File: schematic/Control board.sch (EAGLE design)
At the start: 14 parts, among them IC2 ATTINY44A

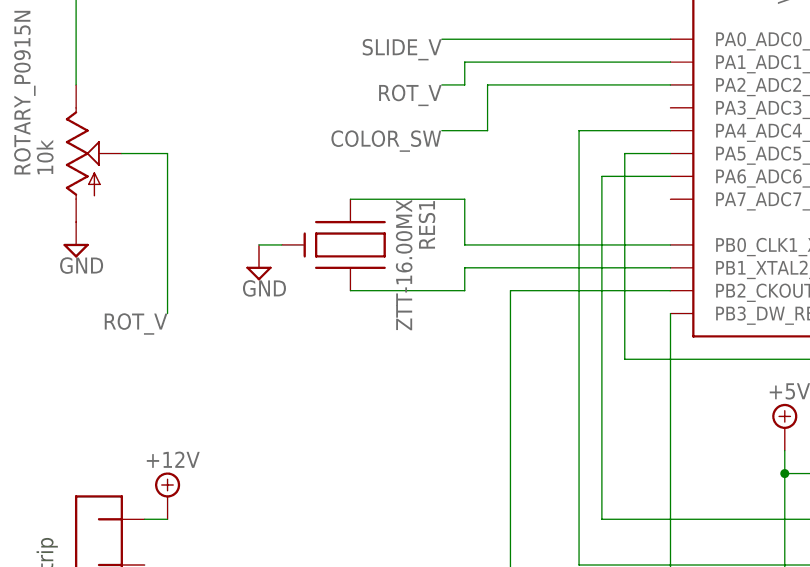
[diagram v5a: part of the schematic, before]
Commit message: Changed the resonator value from 16Mhz to 10MHz, for more accurate LED timing
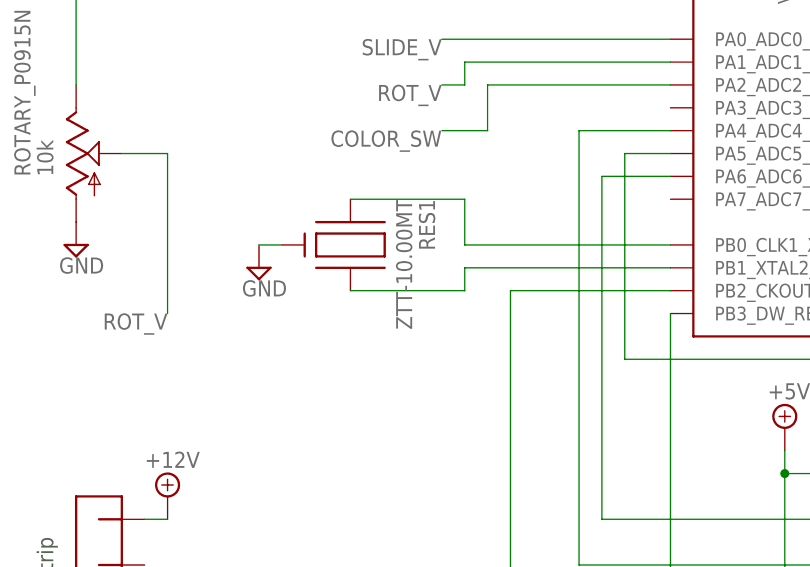
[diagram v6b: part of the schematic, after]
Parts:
- RES1: value ZTT-16.00MX -> ZTT-10.00MT
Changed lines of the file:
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@@
 <part name="SUPPLY11" library="supply2" deviceset="GND" device=""/>
 <part name="SUPPLY12" library="supply2" deviceset="+5V" device=""/>
-<part name="RES1" library="RGB LED project" deviceset="ZTT-16.00MX" device=""/>
+<part name="RES1" library="RGB LED project" deviceset="ZTT-16.00MX" device="" value="ZTT-10.00MT"/>
 <part name="SUPPLY13" library="supply2" deviceset="GND" device=""/>
 <part name="U$1" library="RGB LED project" deviceset="ISP" device=""/>

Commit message: Fixed the bounding area of the potentiometer, and adjusted the value of the reset line's pull-up resistor
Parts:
- R3: value 1M -> 10k
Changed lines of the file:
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@@
 <part name="SUPPLY14" library="supply2" deviceset="+5V" device=""/>
 <part name="SUPPLY15" library="supply2" deviceset="GND" device=""/>
-<part name="R3" library="resistor" deviceset="R-US_" device="0207/7" value="1M"/>
+<part name="R3" library="resistor" deviceset="R-US_" device="0207/7" value="10k"/>
 <part name="SUPPLY16" library="supply2" deviceset="+12V" device=""/>
 <part name="SUPPLY17" library="supply2" deviceset="GND" device=""/>
